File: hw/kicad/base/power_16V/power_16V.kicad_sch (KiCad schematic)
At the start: 34 parts, among them J1 USB_B_Micro, J2 XT30PW-M, J3 TOP, J4 BUTTOM, U1 LM2596S-5, U2 LM1117MP-3.3, U3 CP2104

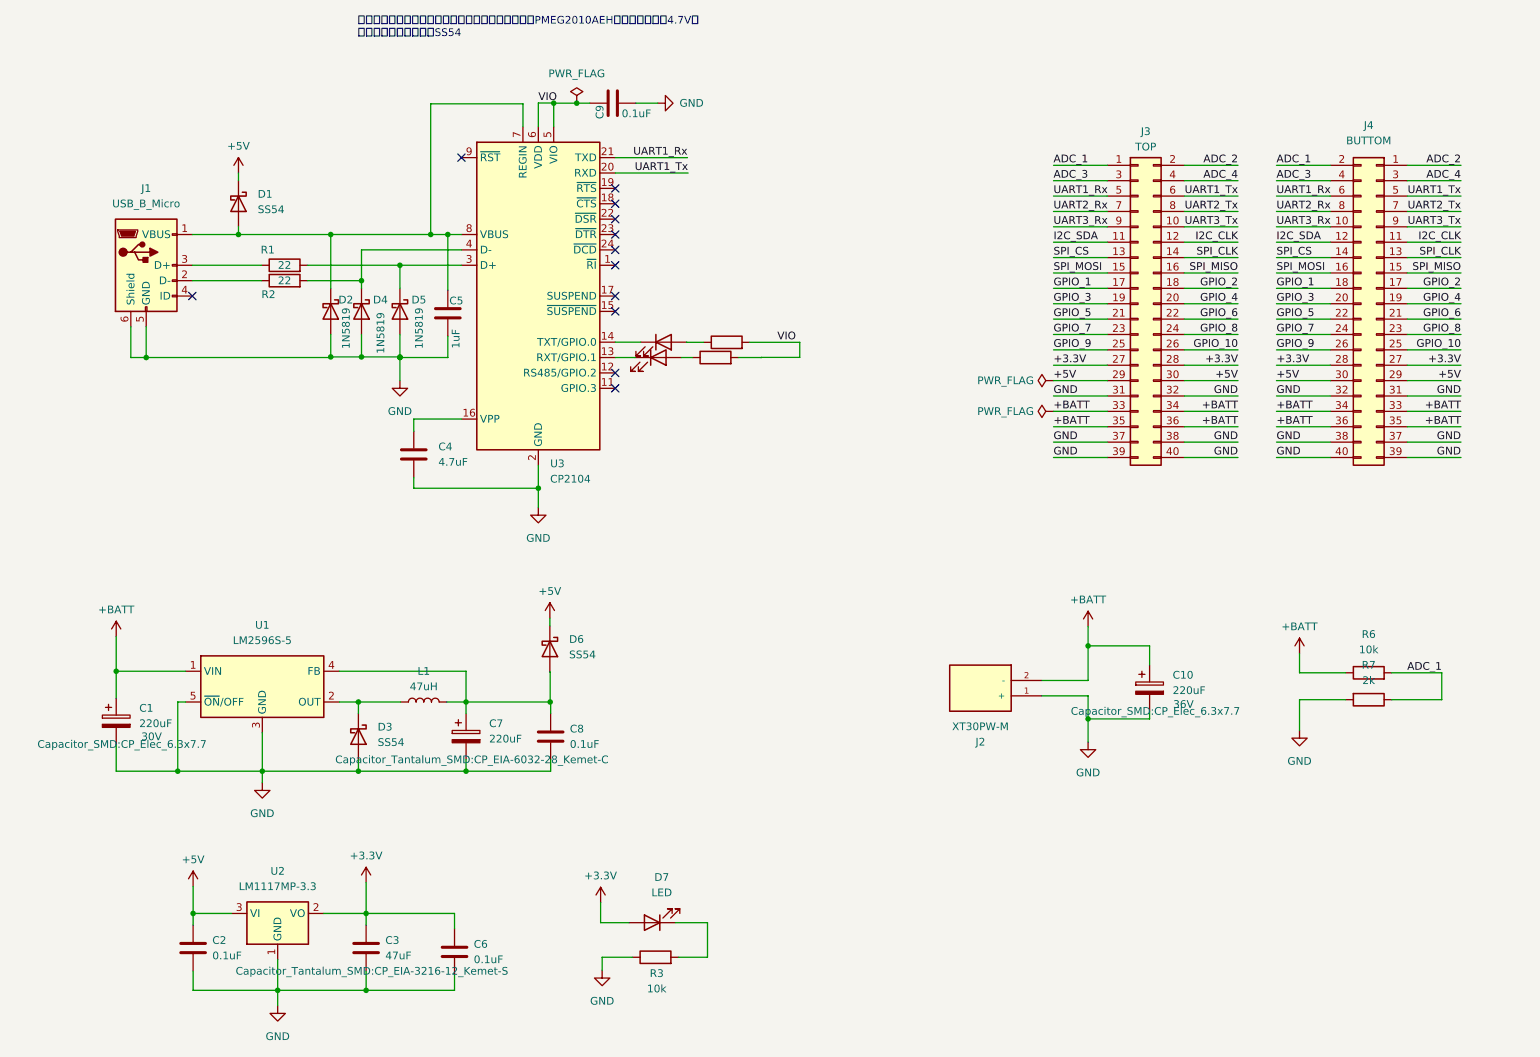
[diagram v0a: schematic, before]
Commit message: 增加电流传感器芯片
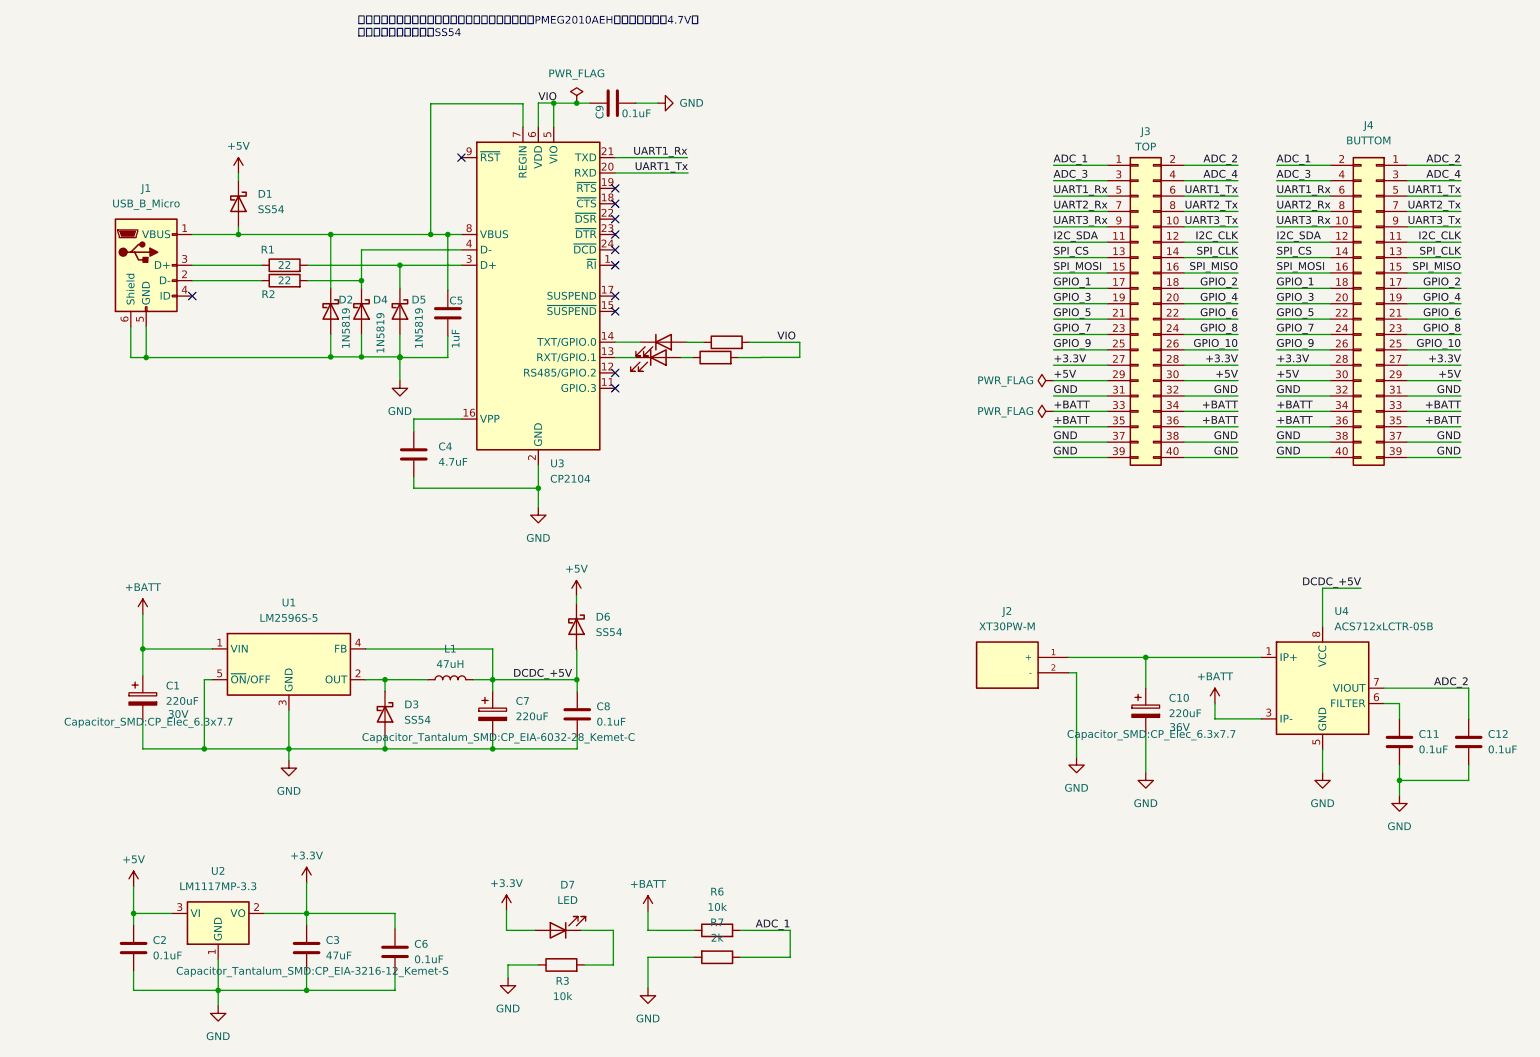
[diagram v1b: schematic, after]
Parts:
- added C11, C12: 0.1uF, Capacitor_SMD:C_0805_2012Metric, symbol Device:C
- added U4: ACS712xLCTR-05B, Package_SO:SOIC-8_3.9x4.9mm_P1.27mm, symbol Sensor_Current:ACS712xLCTR-05B
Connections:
- net +BATT: now also U4.3 (IP-), U4.4 (IP-); no longer C10.1, J2.2 (-)
- net ADC_2: now also C12.1, U4.7 (VIOUT)
- net GND: now also J2.2 (-), C11.2, C12.2, U4.5 (GND); no longer J2.1 (+)
- net DCDC_+5V: now reaches C7.1, C8.1, D6.2 (A), L1.2, U1.4 (FB)
- net DCDC_+5V: now also U4.8 (VCC)
- new net: C10.1, J2.1 (+), U4.1 (IP+), U4.2 (IP+)
- new net: C11.1, U4.6 (FILTER)
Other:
- moved on the sheet: C1, C10, C2, C3, C6, C7, C8, D3, D6, D7, J2, L1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

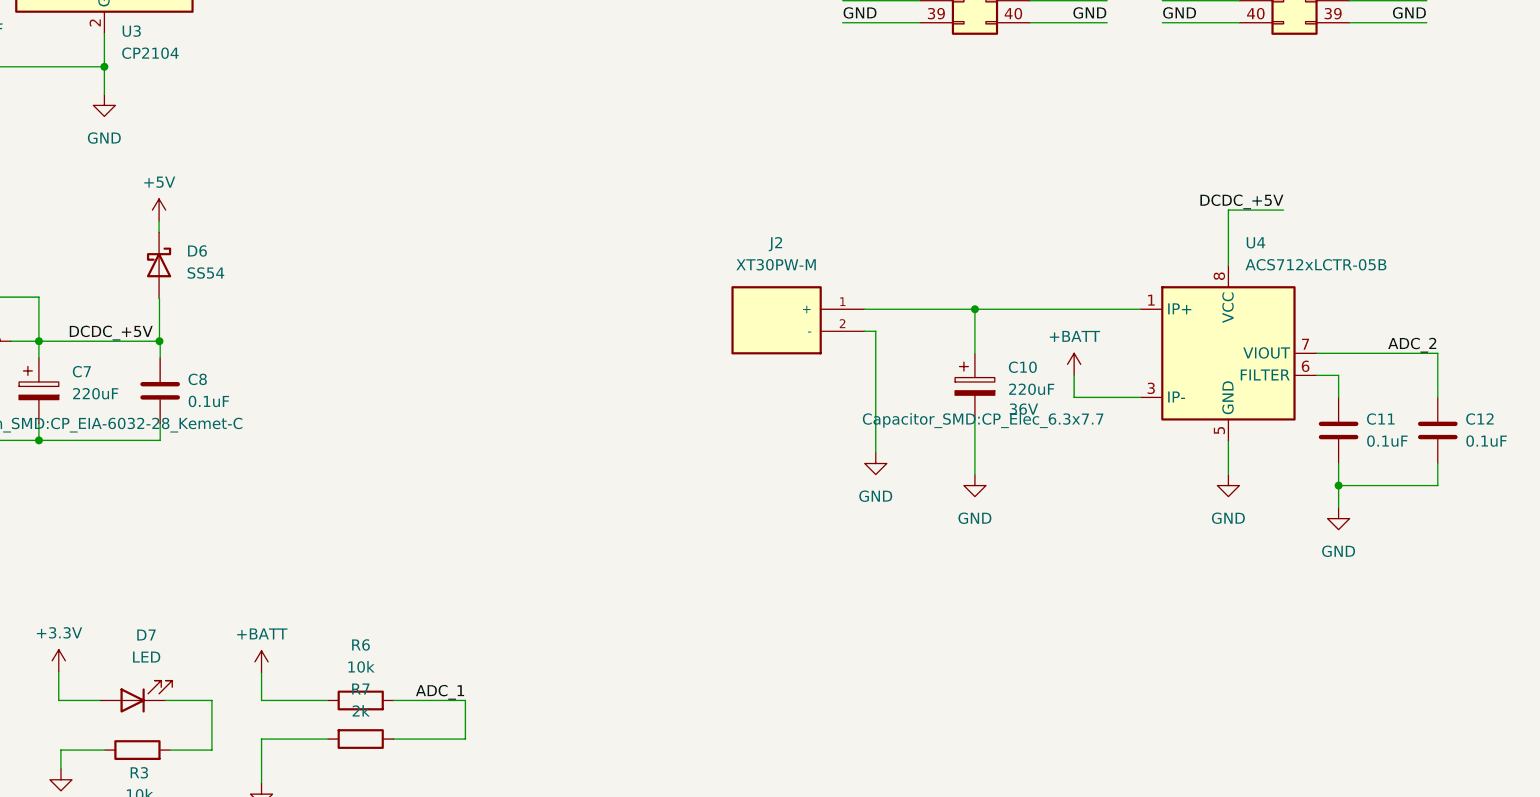
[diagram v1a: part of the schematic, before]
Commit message: 更新power16V板
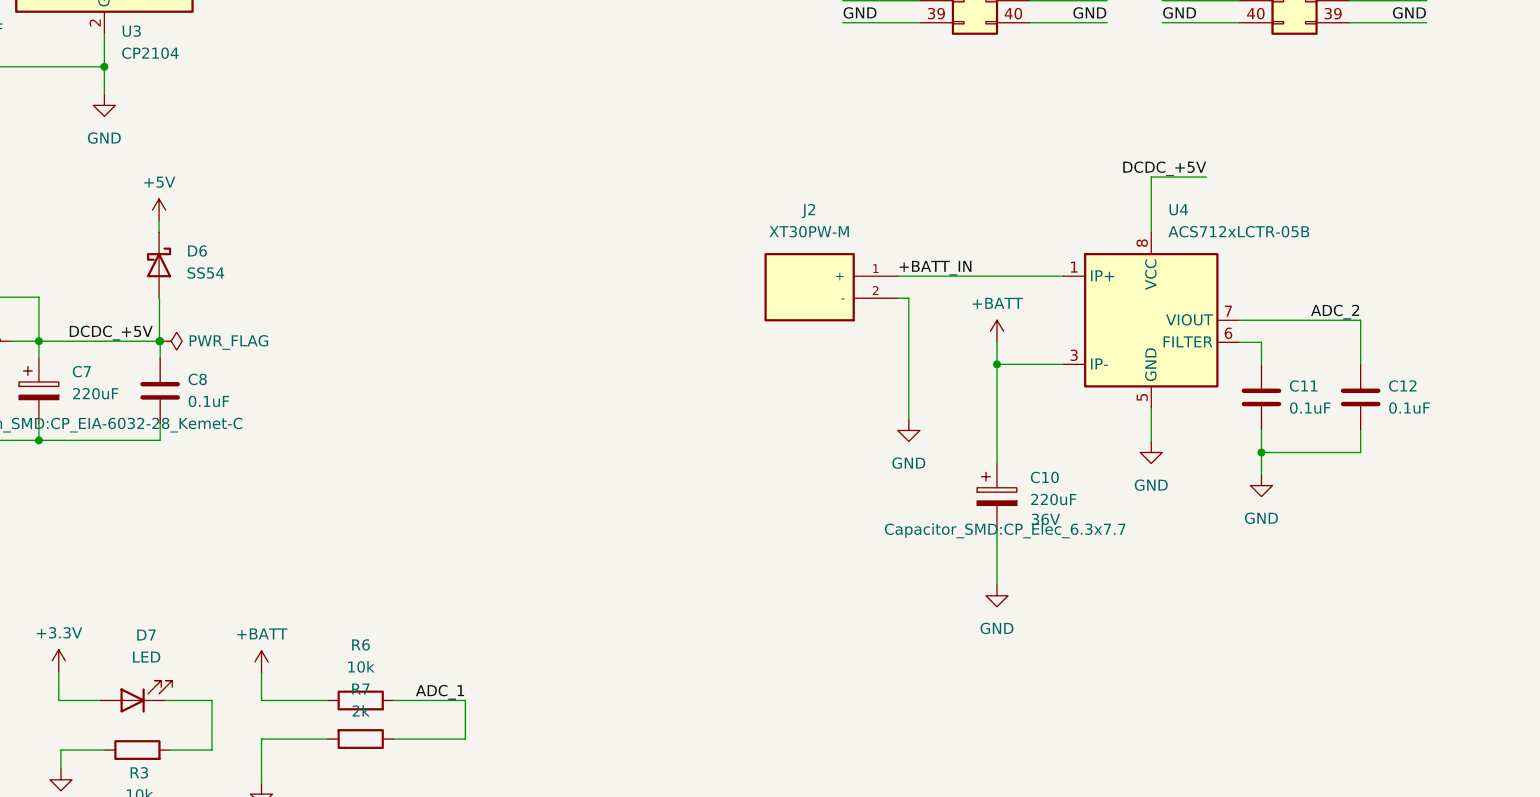
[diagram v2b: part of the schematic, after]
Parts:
- R1, R2: footprint Resistor_SMD:R_0805_2012Metric -> Resistor_SMD:R_0603_1608Metric
- R4, R5: value 22 -> 100
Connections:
- net +BATT: now also C10.1
- net +BATT_IN: now reaches J2.1 (+), U4.1 (IP+), U4.2 (IP+)
- net +BATT_IN: no longer C10.1
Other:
- moved on the sheet: C11, C12, J2, U4

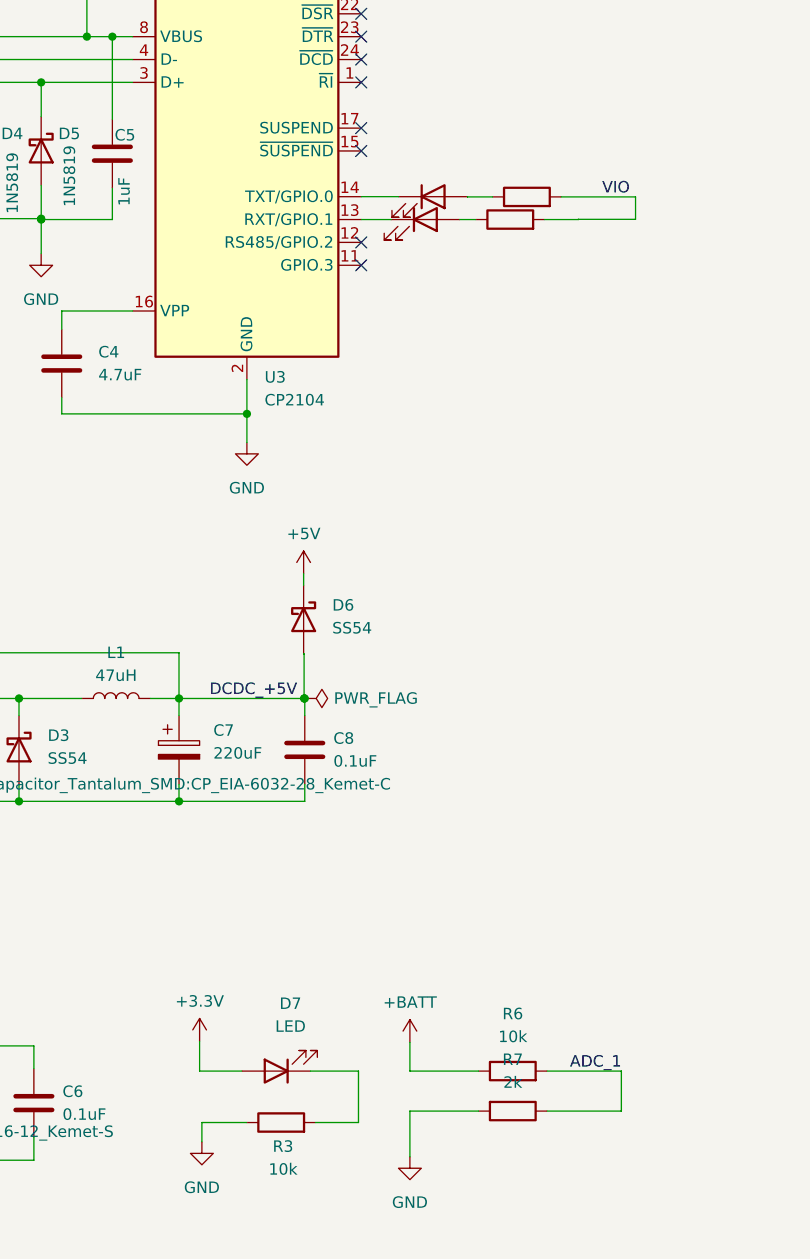
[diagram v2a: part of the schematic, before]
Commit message: 更新power16v一些错误
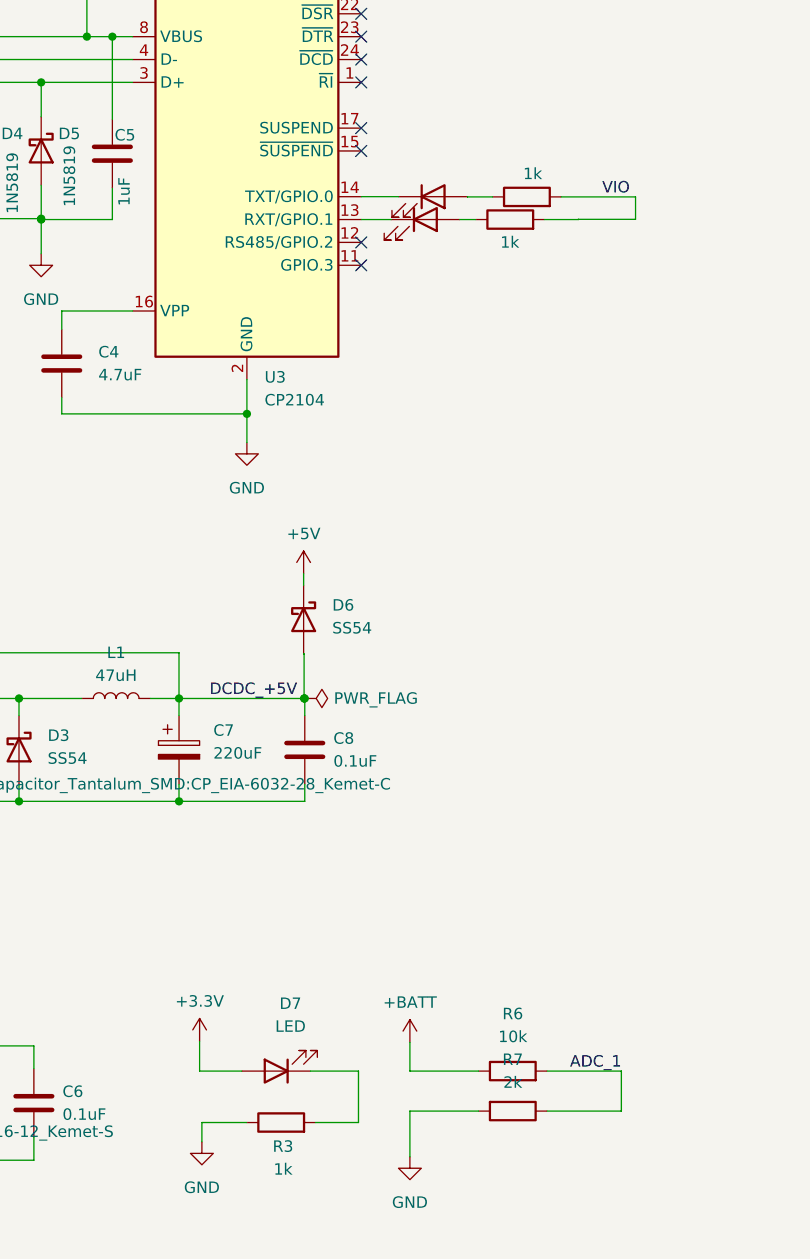
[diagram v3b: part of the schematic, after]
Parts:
- R3: value 10k -> 1k
- R4, R5: value 100 -> 1k
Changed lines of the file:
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@@
       (effects (font (size 1.27 1.27)))
     )
-    (property "Value" "10k" (at 123.3947 177.927 90)
+    (property "Value" "1k" (at 123.3947 177.927 90)
       (effects (font (size 1.27 1.27)))
     )
@@
       (effects (font (size 1.27 1.27)) hide)
     )
-    (property "Value" "100" (at 150.4913 69.8754 90)
-      (effects (font (size 1.27 1.27)) hide)
+    (property "Value" "1k" (at 151.13 67.31 90)
+      (effects (font (size 1.27 1.27)))
     )
     (property "Footprint" "Resistor_SMD:R_0805_2012Metric" (at 150.4913 71.6534 90)
@@
       (effects (font (size 1.27 1.27)) hide)
     )
-    (property "Value" "100" (at 148.6413 72.39 90)
-      (effects (font (size 1.27 1.27)) hide)
+    (property "Value" "1k" (at 148.59 74.93 90)
+      (effects (font (size 1.27 1.27)))
     )
     (property "Footprint" "Resistor_SMD:R_0805_2012Metric" (at 148.6413 74.168 90)

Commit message: 更新USB micro 为优信的封装
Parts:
- J1: footprint Connector_USB:USB_Micro-B_Wuerth_629105150521 -> USB_Micro-B_YouCee:USB_Micro-B_YouCee
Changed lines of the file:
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@@
       (effects (font (size 1.27 1.27)))
     )
-    (property "Footprint" "Connector_USB:USB_Micro-B_Wuerth_629105150521" (at 58.42 58.42 0)
+    (property "Footprint" "USB_Micro-B_YouCee:USB_Micro-B_YouCee" (at 58.42 58.42 0)
       (effects (font (size 1.27 1.27)) hide)
     )
